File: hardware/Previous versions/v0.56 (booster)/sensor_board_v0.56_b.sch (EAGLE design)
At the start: 65 parts, among them J3 USB-MICROB, U1 NEOPIXEL_NANO_2427, U10 TSL2591, U11 915MHz, U12 MH-Z19, U13 CCS811-I2C, U14 IAQ-CORE-C, U15 VLP-450-F, U16 VLP-450-F, U2 FT231XQ-R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

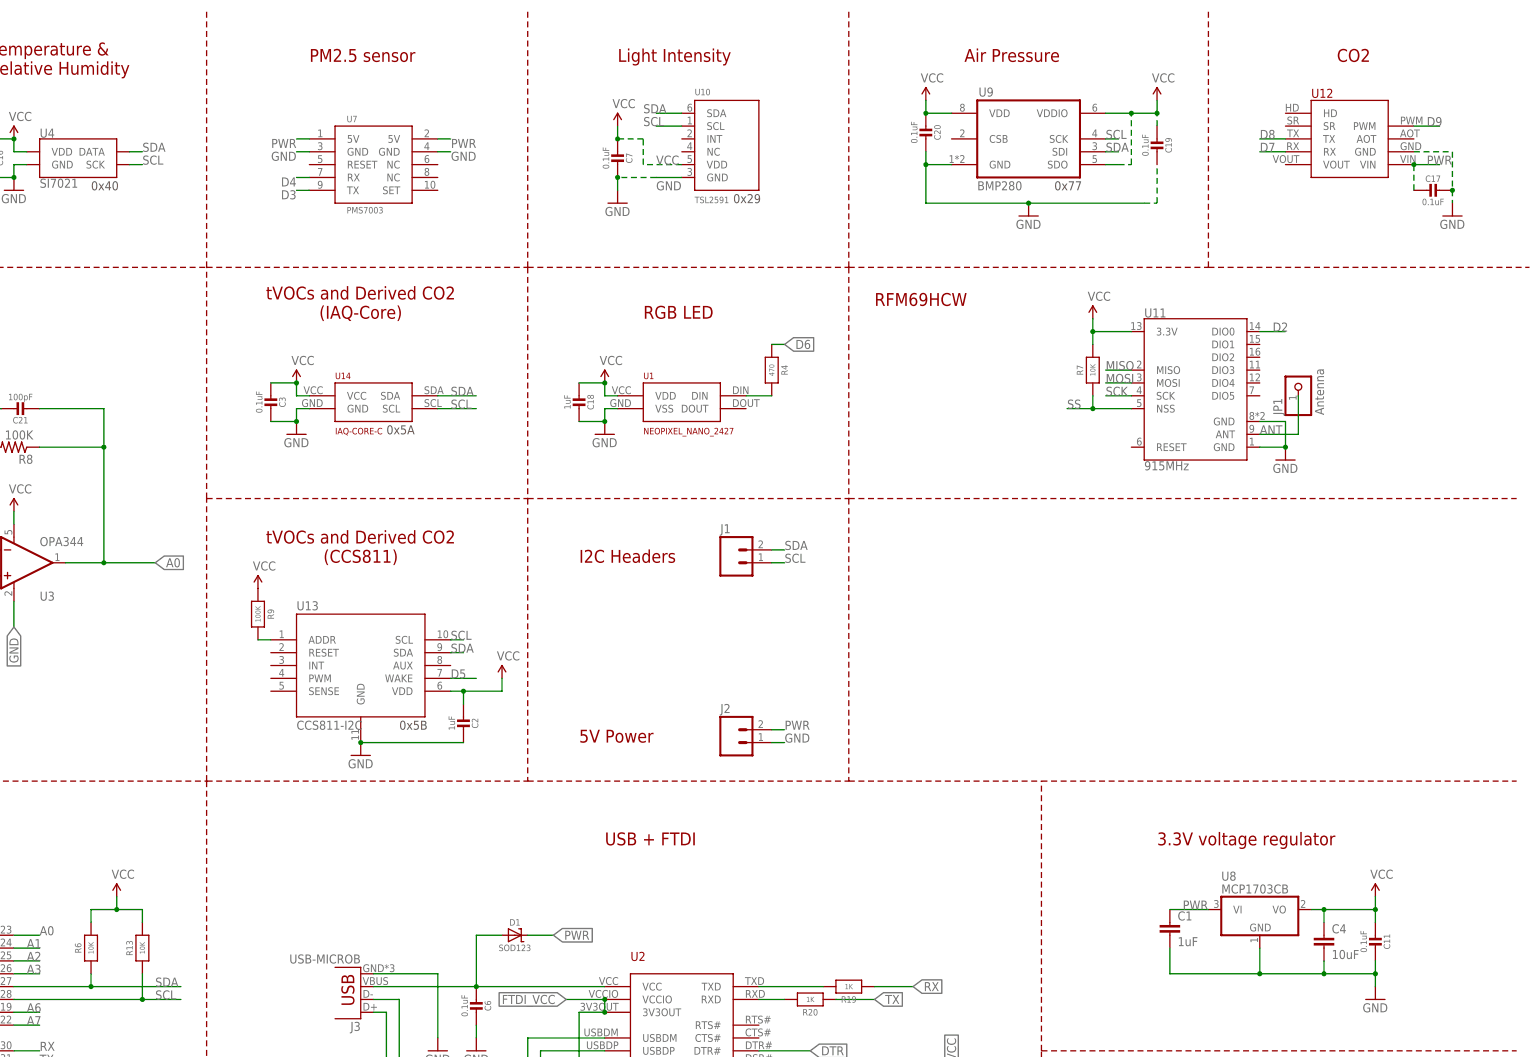
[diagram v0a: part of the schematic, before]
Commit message: v0.56 - completed
DRC & ERC checked
Features:
- Board dimensions and component placement completely redesigned
- Neopixel Mini replaced by NeoPixel Nano 2427
- Light pipes for NeoPixel and Light sensor
- SHT31 replaced with Si7021
- Added three mounting holes
- Cutout for the helical antenna
- CCS811 VOC sensor added
- MH-z19 CO2 sensor pads added (can be replaced with IAQ core - pads
also available) (can also be replaced by S8 CO2 sensor in future for
larger orders)
- ATMEGA328P-AU replaced by ATMEGA328P-MU (QFN)
- FT232RL replaced by FT231XQ (QFN)
- Notches in PCB for attaching to enclosure
- 0805 Diode replaced with SOD123
- ISP headers replaced with TagConnect
- Better thermal isolation for T/RH sensor
- I2C & power headers moved to left
- Several 0805 components replaced by 0402 ones
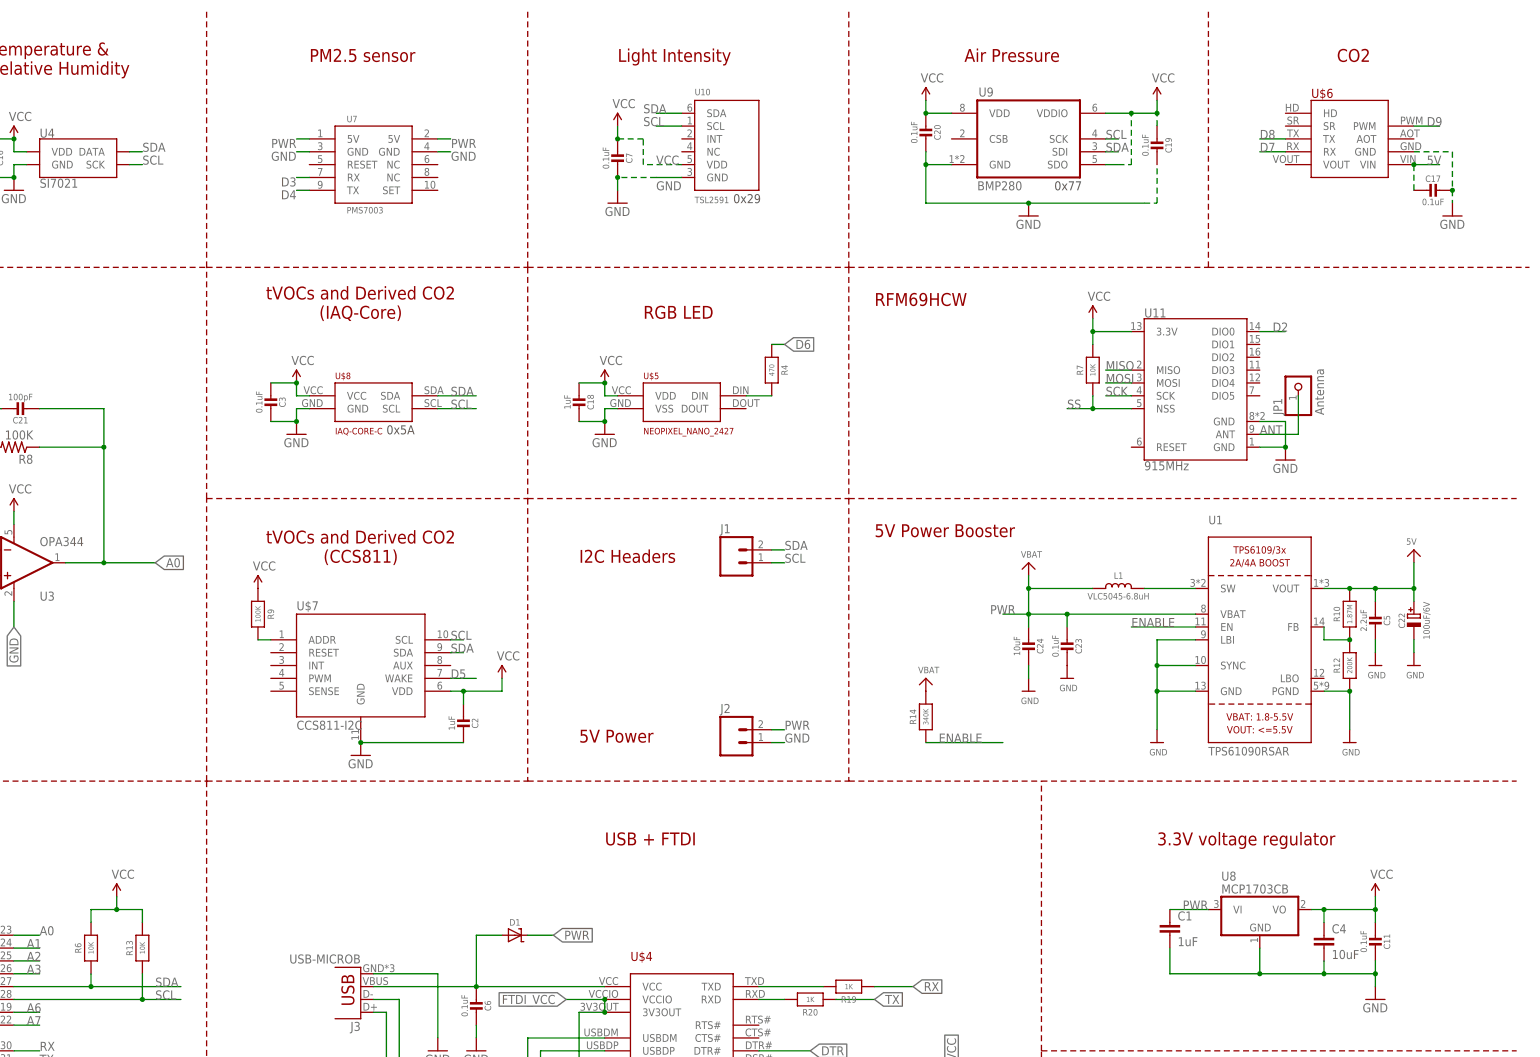
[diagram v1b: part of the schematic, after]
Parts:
- added C22: 100uF/6V, microbuilder:CAP_TANTALUMB/3528_REFLOW
- added C23: 0.1uF, Adafruit Feather 32u4 Bluefruit LE:MICROBUILDER_CAP_CERAMIC_0402MP
- added C24: 10uF, Adafruit Feather 32u4 Bluefruit LE:MICROBUILDER_CAP_CERAMIC_0402MP
- added C5: 2.2uF, Adafruit Feather 32u4 Bluefruit LE:MICROBUILDER_CAP_CERAMIC_0402MP
- added L1: VLC5045-6.8uH, microbuilder:INDUCTORTDK_VLC5045
- added R10: 1.87M, Adafruit Feather 32u4 Bluefruit LE:MICROBUILDER_RESISTOR_0402MP
- added R12: 200K, Adafruit Feather 32u4 Bluefruit LE:MICROBUILDER_RESISTOR_0402MP
- added R14: 340K, Adafruit Feather 32u4 Bluefruit LE:MICROBUILDER_RESISTOR_0402MP
- added U$5: NEOPIXEL_NANO_2427, NeoPixel Nano 2427:NEOPIXEL_NANO_2427
- D1: value SOD123 -> (none)
- U1: value NEOPIXEL_NANO_2427 -> TPS61090RSAR; device NeoPixel Nano 2427:NEOPIXEL_NANO_2427 -> microbuilder:VREG_TPS6103X
- renumbered U12 to U$6, U13 to U$7, U14 to U$8, U15 to U$9, U16 to U$12, U2 to U$4
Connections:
- new net 5V: C17.2, C22.+, C5.2, R10.2, U$6.VIN, U1.VOUT
- new net ENABLE: R14.1, U1.EN
- new net N$12: R10.1, R12.2, U1.FB
- new net N$6: L1.2, U1.SW
- new net VBAT: R14.2
- net D3: now also U7.RX; no longer U7.TX
- net D4: now also U7.TX; no longer U7.RX
- net GND: now also C22.-, C23.1, C24.1, C5.1, R12.1, U$5.VSS, U1.GND, U1.LBI, U1.PGND, U1.SYNC; no longer U1.VSS
- net N$1: now also U$5.DIN; no longer U1.DIN
- net PWR: now also C23.2, C24.2, L1.1, U1.VBAT; no longer C17.2, U$6.VIN
- net VCC: now also U$5.VDD; no longer U1.VDD
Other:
- note added: "5V Power Booster"
- note removed: "0x40"
- note removed: "0x5B"
